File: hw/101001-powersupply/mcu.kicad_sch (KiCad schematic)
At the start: 15 parts, among them U401 ESP32-C3-MINI-1

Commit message: Progress on board design
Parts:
- added R408, R409: 0Ohm, Resistor_SMD:R_0402_1005Metric, symbol Device:R
- renumbered R408 to R410, R409 to R411, R410 to R412, R411 to R413
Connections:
- net VPROG_MEAS: now also U401.13 (GPIO1/ADC1_CH1/XTAL_32K_N), R409.1; no longer U401.12 (GPIO0/ADC1_CH0/XTAL_32K_P)
- net VSUPPLY_MEAS: now also U401.12 (GPIO0/ADC1_CH0/XTAL_32K_P), R408.2; no longer U401.13 (GPIO1/ADC1_CH1/XTAL_32K_N)
- new net GPIO0: R408.1
- new net GPIO1: R409.2
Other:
- company: (none) -> Sarif
- title: (none) -> Variable USB power supply
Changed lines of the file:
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@@
 	(generator_version "8.0")
 	(paper "A4")
+	(title_block
+		(title "Variable USB power supply")
+		(date "2024-04-23")
+		(rev "1")
+		(company "Sarif")
+	)
 	(junction
 		(at 143.51 43.18)
@@
 	(wire
 		(pts
+			(xy 116.84 167.64) (xy 127 167.64)
+		)
+		(stroke
+			(width 0)
+			(type default)
+		)
+	)
+	(wire
+		(pts
 			(xy 238.76 40.64) (xy 234.95 40.64)
 		)
@@
 	(wire
 		(pts
+			(xy 116.84 165.1) (xy 127 165.1)
+		)
+		(stroke
+			(width 0)
+			(type default)
+		)
+	)
+	(wire
+		(pts
+			(xy 134.62 165.1) (xy 153.67 165.1)
+		)
+		(stroke
+			(width 0)
+			(type default)
+		)
+	)
+	(wire
+		(pts
 			(xy 143.51 71.12) (xy 148.59 71.12)
 		)
@@
 		(pts
 			(xy 234.95 40.64) (xy 234.95 48.26)
+		)
+		(stroke
+			(width 0)
+			(type default)
+		)
+	)
+	(wire
+		(pts
+			(xy 134.62 167.64) (xy 153.67 167.64)
 		)
 		(stroke
@@
 		)
 	)
-	(label "EN"
-		(at 34.29 45.72 180)
+	(label "VPROG_MEAS"
+		(at 153.67 167.64 180)
 		(fields_autoplaced yes)
 		(effects
@@
 		)
 	)
-	(label "VOUT_MEAS"
-		(at 203.2 111.76 180)
+	(label "EN"
+		(at 34.29 45.72 180)
 		(fields_autoplaced yes)
 		(effects
@@
 	)
 	(label "VSUPPLY_MEAS"
-		(at 111.76 91.44 0)
+		(at 153.67 165.1 180)
 		(fields_autoplaced yes)
 		(effects
@@
 				(size 1.27 1.27)
 			)
-			(justify left bottom)
+			(justify right bottom)
 		)
 	)
 	(label "VOUT_MEAS"
-		(at 67.31 153.67 180)
+		(at 203.2 111.76 180)
 		(fields_autoplaced yes)
 		(effects
@@
 	)
 	(label "VSUPPLY_MEAS"
-		(at 67.31 151.13 180)
+		(at 111.76 88.9 0)
 		(fields_autoplaced yes)
 		(effects
@@
 				(size 1.27 1.27)
 			)
-			(justify right bottom)
-		)
-	)
-	(label "VPROG_MEAS"
-		(at 67.31 148.59 180)
+			(justify left bottom)
+		)
+	)
+	(label "VOUT_MEAS"
+		(at 67.31 153.67 180)
 		(fields_autoplaced yes)
 		(effects
@@
 		)
 	)
-	(label "EN"
-		(at 124.46 83.82 0)
+	(label "VSUPPLY_MEAS"
+		(at 67.31 151.13 180)
 		(fields_autoplaced yes)
 		(effects
@@
 				(size 1.27 1.27)
 			)
-			(justify left bottom)
+			(justify right bottom)
 		)
 	)
 	(label "VPROG_MEAS"
-		(at 111.76 88.9 0)
+		(at 67.31 148.59 180)
 		(fields_autoplaced yes)
 		(effects
@@
 				(size 1.27 1.27)
 			)
+			(justify right bottom)
+		)
+	)
+	(label "EN"
+		(at 124.46 83.82 0)
+		(fields_autoplaced yes)
+		(effects
+			(font
+				(size 1.27 1.27)
+			)
 			(justify left bottom)
+		)
+	)
+	(label "VPROG_MEAS"
+		(at 111.76 91.44 0)
+		(fields_autoplaced yes)
+		(effects
+			(font
+				(size 1.27 1.27)
+			)
+			(justify left bottom)
+		)
+	)
+	(hierarchical_label "GPIO1"
+		(shape bidirectional)
+		(at 116.84 167.64 180)
+		(fields_autoplaced yes)
+		(effects
+			(font
+				(size 1.27 1.27)
+			)
+			(justify right)
 		)
 	)
@@
 			)
 			(justify left)
+		)
+	)
+	(hierarchical_label "GPIO0"
+		(shape bidirectional)
+		(at 116.84 165.1 180)
+		(fields_autoplaced yes)
+		(effects
+			(font
+				(size 1.27 1.27)
+			)
+			(justify right)
 		)
 	)
@@
 		(on_board yes)
 		(dnp no)
-		(property "Reference" "R408"
+		(property "Reference" "R410"
 			(at 226.06 48.26 90)
 			(effects
@@
 			(project "101001-powersupply"
 				(path "/5b6c9e65-6d2e-4a49-a6e0-6edf7b37266c/9dba7326-5b24-45b7-989c-2d4d44bf0404"
-					(reference "R408")
+					(reference "R410")
 					(unit 1)
 				)
@@
 	)
 	(symbol
+		(lib_id "Device:R")
+		(at 130.81 167.64 270)
+		(unit 1)
+		(exclude_from_sim no)
+		(in_bom no)
+		(on_board yes)
+		(dnp yes)
+		(property "Reference" "R409"
+			(at 128.27 170.18 90)
+			(effects
+				(font
+					(size 1.27 1.27)
+				)
+				(justify left top)
+			)
+		)
+		(property "Value" "0Ohm"
+			(at 128.27 172.72 90)
+			(effects
+				(font
+					(size 1.27 1.27)
+				)
+				(justify left top)
+			)
+		)
+		(property "Footprint" "Resistor_SMD:R_0402_1005Metric"
+			(at 130.81 165.862 90)
+			(effects
+				(font
+					(size 1.27 1.27)
+				)
+				(hide yes)
+			)
+		)
+		(property "Datasheet" "~"
+			(at 130.81 167.64 0)
+			(effects
+				(font
+					(size 1.27 1.27)
+				)
+				(hide yes)
+			)
+		)
+		(property "Description" ""
+			(at 130.81 167.64 0)
+			(effects
+				(font
+					(size 1.27 1.27)
+				)
+				(hide yes)
+			)
+		)
+		(pin "1"
+		)
+		(pin "2"
+		)
+		(instances
+			(project "101001-powersupply"
+				(path "/5b6c9e65-6d2e-4a49-a6e0-6edf7b37266c/9dba7326-5b24-45b7-989c-2d4d44bf0404"
+					(reference "R409")
+					(unit 1)
+				)
+			)
+		)
+	)
+	(symbol
 		(lib_id "Device:C")
 		(at 27.94 52.07 180)
@@
 		(on_board yes)
 		(dnp no)
-		(property "Reference" "R410"
+		(property "Reference" "R412"
 			(at 233.68 48.26 90)
 			(effects
@@
 			(project "101001-powersupply"
 				(path "/5b6c9e65-6d2e-4a49-a6e0-6edf7b37266c/9dba7326-5b24-45b7-989c-2d4d44bf0404"
-					(reference "R410")
+					(reference "R412")
 					(unit 1)
 				)
@@
 		(on_board yes)
 		(dnp no)
-		(property "Reference" "R411"
+		(property "Reference" "R413"
 			(at 237.49 48.26 90)
 			(effects
@@
 			(project "101001-powersupply"
 				(path "/5b6c9e65-6d2e-4a49-a6e0-6edf7b37266c/9dba7326-5b24-45b7-989c-2d4d44bf0404"
-					(reference "R411")
+					(reference "R413")
 					(unit 1)
 				)
@@
 	(symbol
 		(lib_id "Device:R")
+		(at 130.81 165.1 90)
+		(unit 1)
+		(exclude_from_sim no)
+		(in_bom no)
+		(on_board yes)
+		(dnp yes)
+		(property "Reference" "R408"
+			(at 128.27 160.02 90)
+			(effects
+				(font
+					(size 1.27 1.27)
+				)
+				(justify right top)
+			)
+		)
+		(property "Value" "0Ohm"
+			(at 128.27 162.56 90)
+			(effects
+				(font
+					(size 1.27 1.27)
+				)
+				(justify right top)
+			)
+		)
+		(property "Footprint" "Resistor_SMD:R_0402_1005Metric"
+			(at 130.81 166.878 90)
+			(effects
+				(font
+					(size 1.27 1.27)
+				)
+				(hide yes)
+			)
+		)
+		(property "Datasheet" "~"
+			(at 130.81 165.1 0)
+			(effects
+				(font
+					(size 1.27 1.27)
+				)
+				(hide yes)
+			)
+		)
+		(property "Description" ""
+			(at 130.81 165.1 0)
+			(effects
+				(font
+					(size 1.27 1.27)
+				)
+				(hide yes)
+			)
+		)
+		(pin "1"
+		)
+		(pin "2"
+		)
+		(instances
+			(project "101001-powersupply"
+				(path "/5b6c9e65-6d2e-4a49-a6e0-6edf7b37266c/9dba7326-5b24-45b7-989c-2d4d44bf0404"
+					(reference "R408")
+					(unit 1)
+				)
+			)
+		)
+	)
+	(symbol
+		(lib_id "Device:R")
 		(at 231.14 52.07 180)
 		(unit 1)
@@
 		(on_board yes)
 		(dnp no)
-		(property "Reference" "R409"
+		(property "Reference" "R411"
 			(at 229.87 48.26 90)
 			(effects
@@
 			(project "101001-powersupply"
 				(path "/5b6c9e65-6d2e-4a49-a6e0-6edf7b37266c/9dba7326-5b24-45b7-989c-2d4d44bf0404"
-					(reference "R409")
+					(reference "R411")
 					(unit 1)
 				)

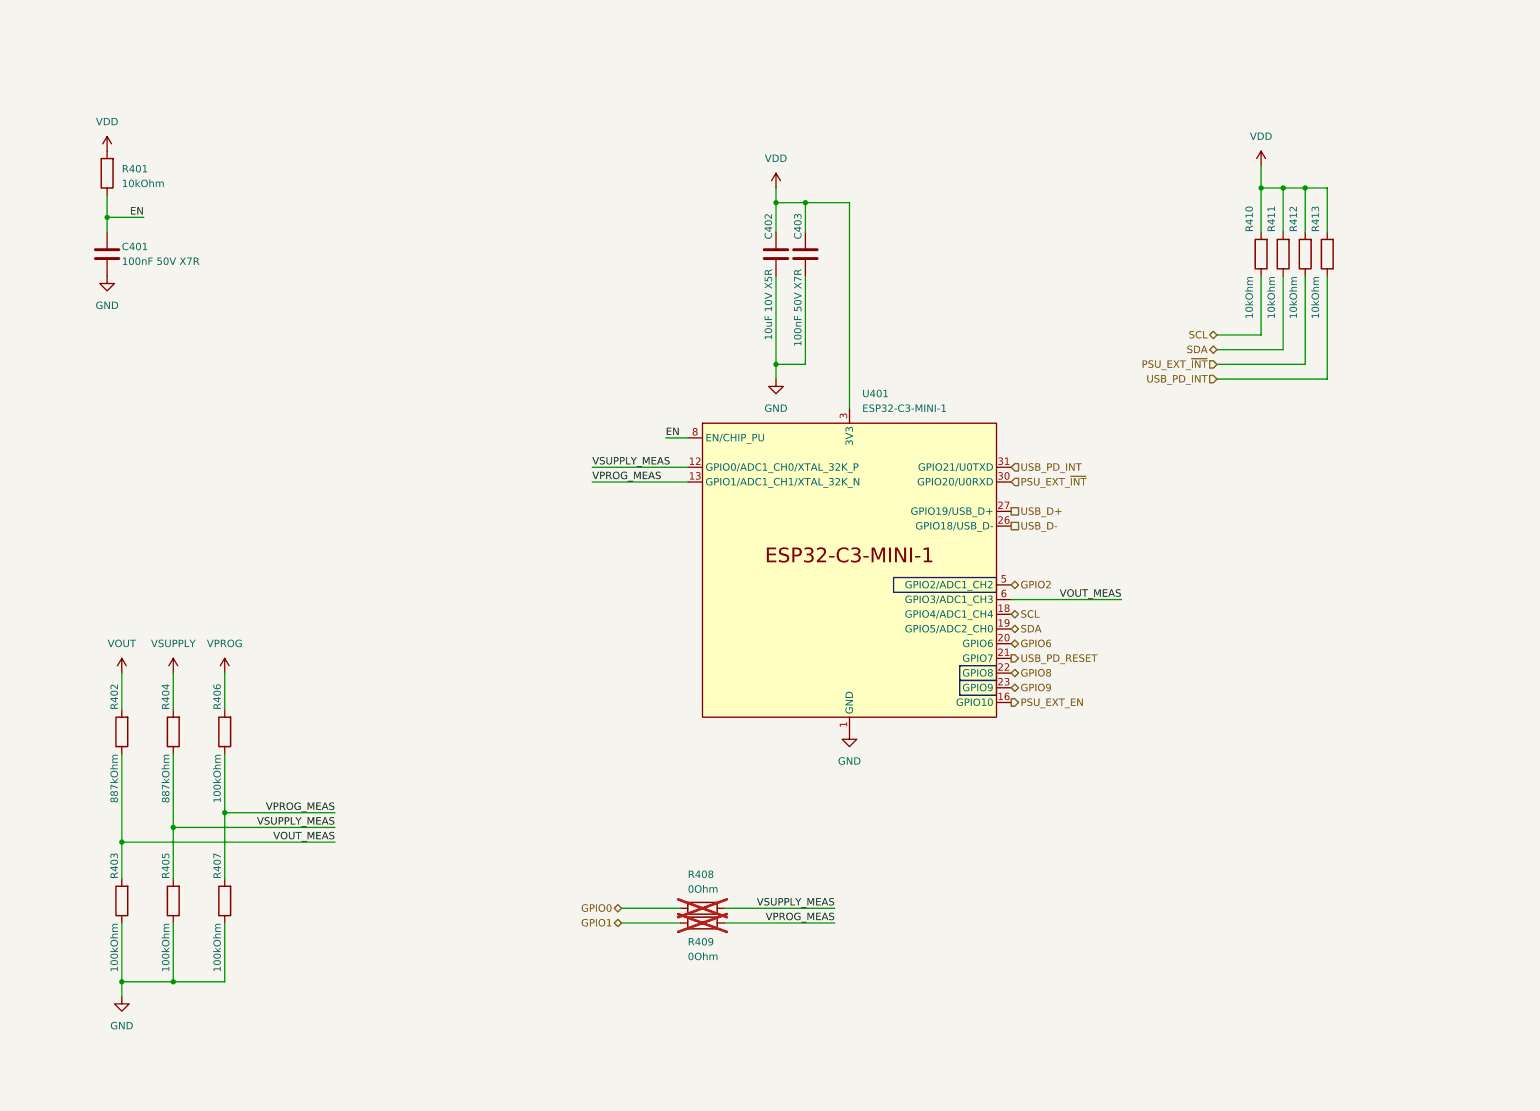
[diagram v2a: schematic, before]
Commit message: Added strapping pins bias and buttons
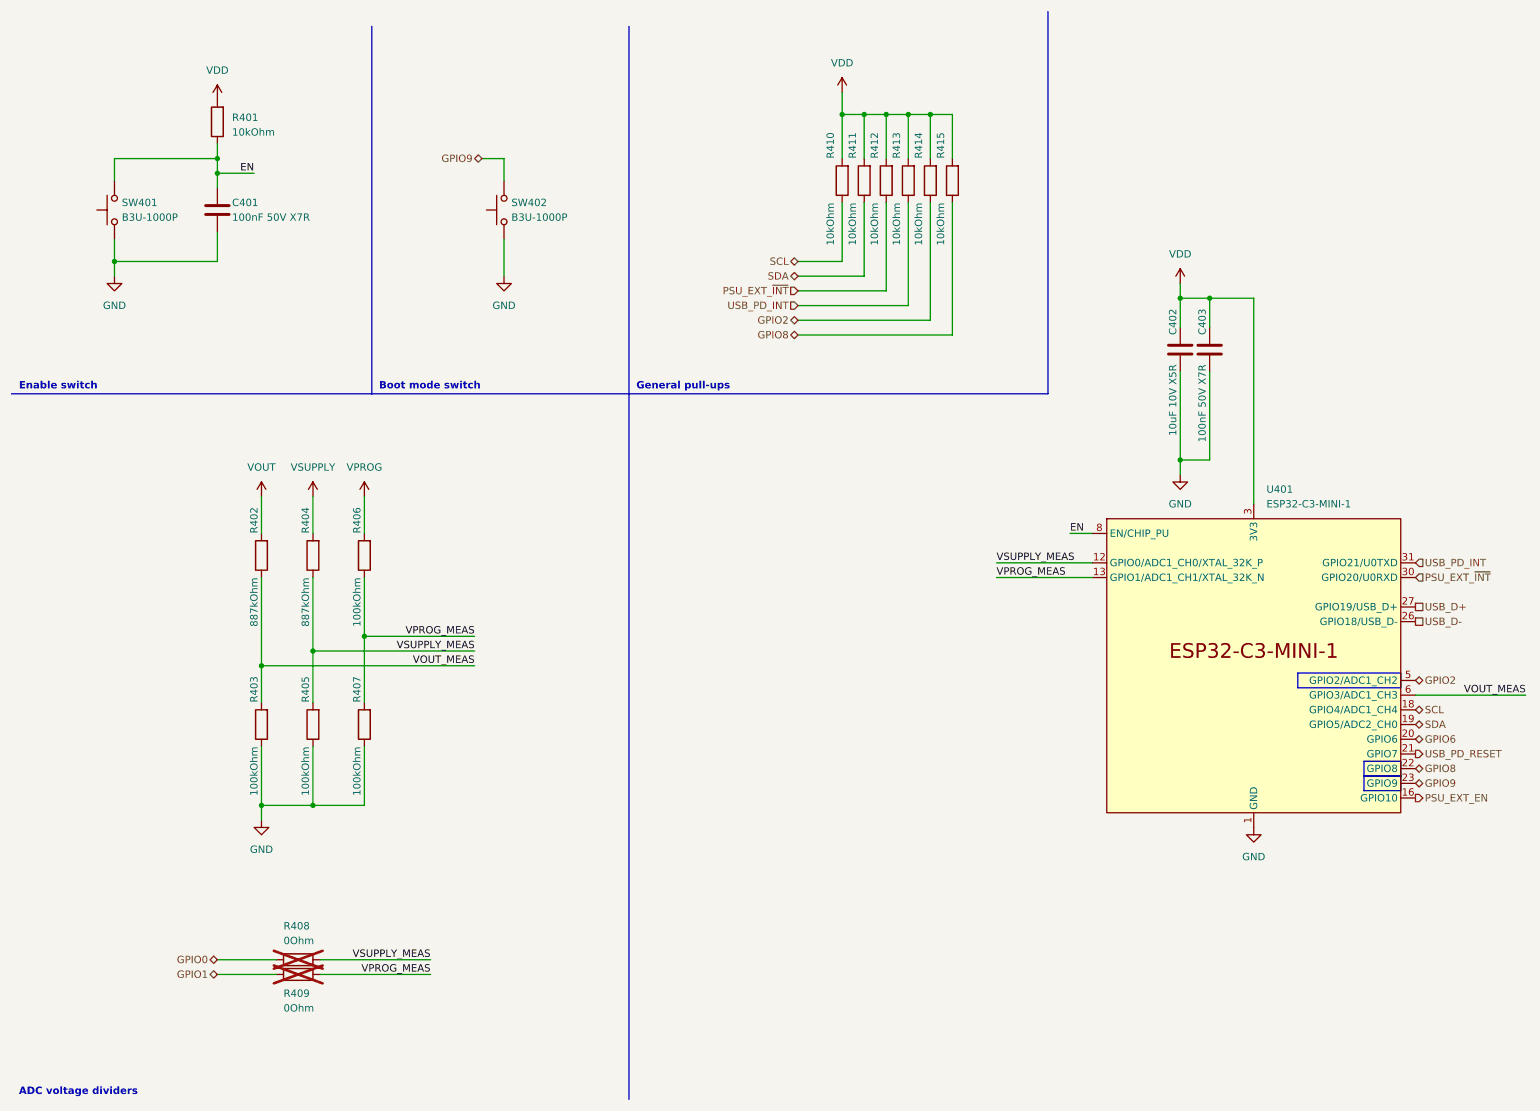
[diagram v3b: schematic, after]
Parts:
- added R414, R415: 10kOhm, Resistor_SMD:R_0402_1005Metric, symbol Device:R
- added SW401, SW402: B3U-1000P, Button_Switch_SMD:SW_SPST_B3U-1000P, symbol Switch:SW_Push
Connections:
- net EN: now also SW401.2
- net GND: now also SW401.1, SW402.1
- net GPIO2: now also R414.1
- net GPIO8: now also R415.1
- net GPIO9: now also SW402.2
- net VDD: now also R414.2, R415.2
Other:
- note added: "ADC voltage dividers"
- note added: "Boot mode switch"
- note added: "Enable switch"
- note added: "General pull-ups"
- moved on the sheet: C401, C402, C403, R401, R402, R403, R404, R405, R406, R407, R408, R409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
